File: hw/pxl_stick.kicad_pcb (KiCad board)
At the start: 2 copper layers, 25 x 99.9 mm, 60 parts, among them J1 Conn_01x02, J2 Conn_01x06_Socket, J3 Conn_01x01_Socket, J4 Conn_01x01, Q1 IRLML6244, Q2 IRLML6244, U1 AP2112K-3.3, U2 TSOP75438WTT, U3 INMP441ACEZ-R7, U4 ESP32-WROOM-E, U5 SN74LVC1T45DCK

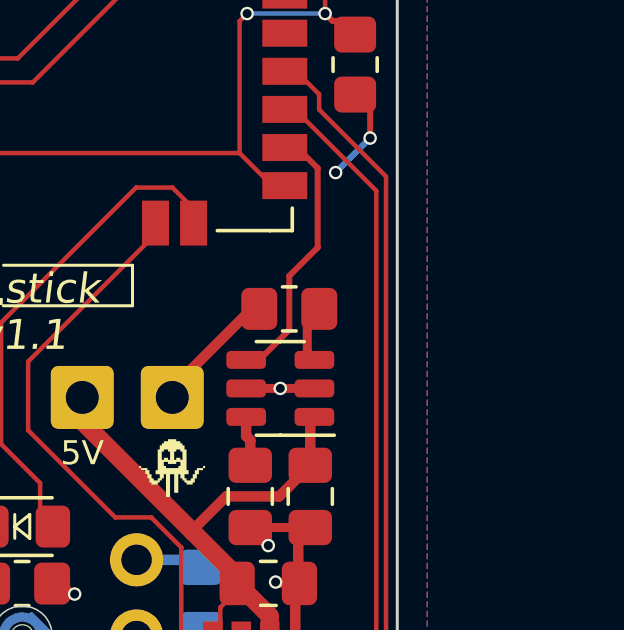
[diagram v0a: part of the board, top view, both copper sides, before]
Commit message: Add footprint for 2 channel level shifter
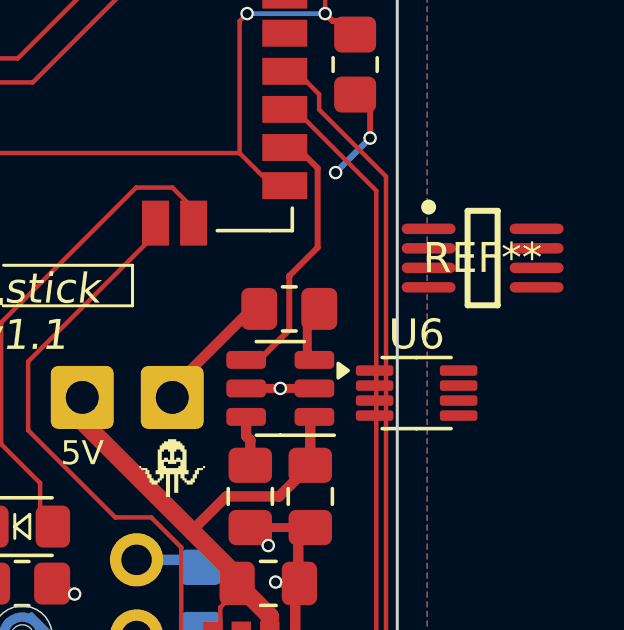
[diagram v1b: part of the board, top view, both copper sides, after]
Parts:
- added REF**: DCT0008A_N, footprints:DCT0008A_M, F.Cu at (88.7, 101.8)
- added U6: SN74LVC2T45DCUR, Package_SO:VSSOP-8_2.3x2mm_P0.5mm, F.Cu at (86.5, 106.3)
- R13, R14, R3, R4, R5, R9: value 10k -> 20k
